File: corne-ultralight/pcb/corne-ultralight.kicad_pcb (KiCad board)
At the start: 2 copper layers, 275.5 x 105.6 mm, 136 parts, among them J2 OLED, J5 Breakaway_Tabs, J7 OLED, SW1 SW_PUSH, SW10 SW_PUSH, SW11 SW_PUSH, SW12 SW_PUSH, SW13 SW_PUSH, SW14 SW_PUSH, SW15 SW_PUSH, SW16 SW_PUSH, SW17 SW_PUSH, SW18 SW_PUSH, SW19 SW_PUSH, SW2 SW_PUSH, SW20 SW_PUSH, SW21 SW_PUSH, SW22 SW_PUSH, SW23 SW_PUSH, SW24 SW_PUSH, SW25 SW_PUSH, SW26 SW_PUSH, SW27 SW_PUSH, SW28 SW_PUSH, SW29 SW_PUSH, SW3 SW_PUSH, SW30 SW_PUSH, SW31 SW_PUSH, SW32 SW_PUSH, SW33 SW_PUSH, SW34 SW_PUSH, SW35 SW_PUSH, SW36 SW_PUSH, SW37 SW_PUSH, SW38 SW_PUSH, SW39 SW_PUSH, SW4 SW_PUSH, SW40 SW_PUSH, SW41 SW_PUSH, SW42 SW_PUSH, SW5 SW_PUSH, SW6 SW_PUSH, SW7 SW_PUSH, SW8 SW_PUSH, SW9 SW_PUSH, U1 ProMicro, U2 ProMicro

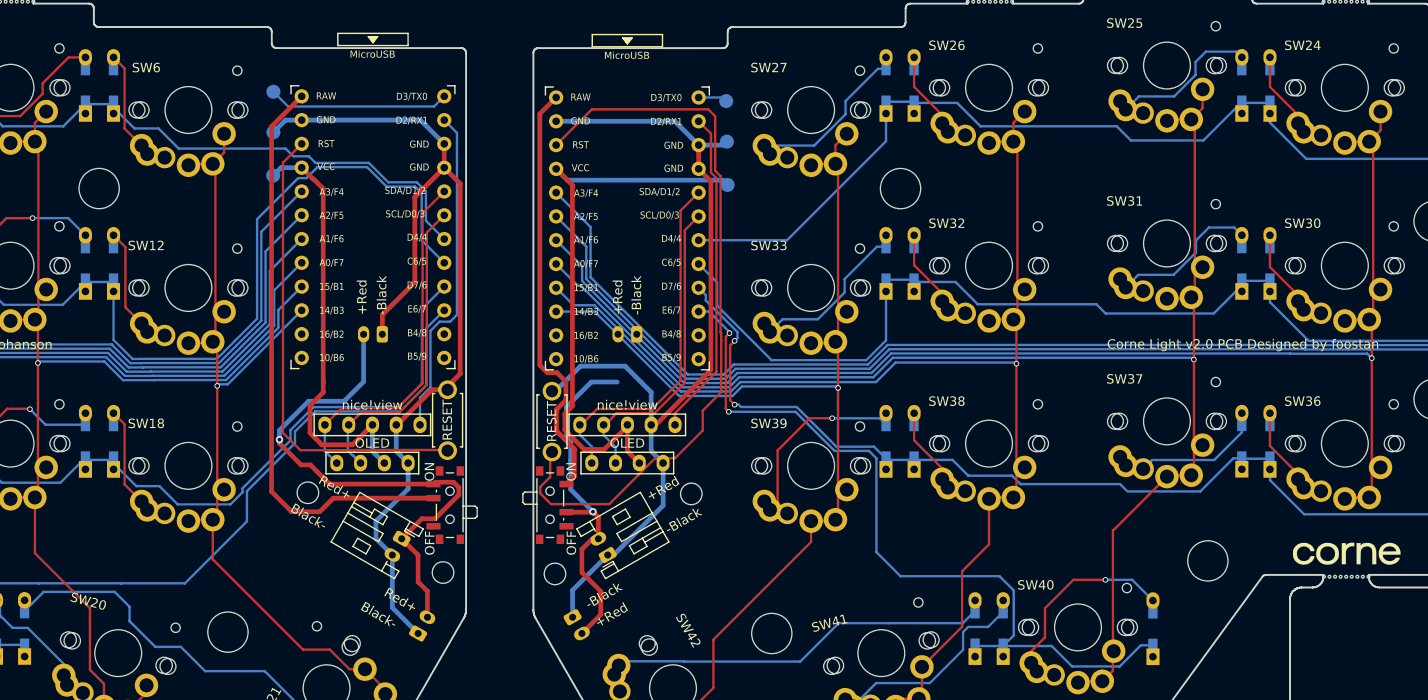
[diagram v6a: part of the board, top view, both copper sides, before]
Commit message: Holes for battery cables
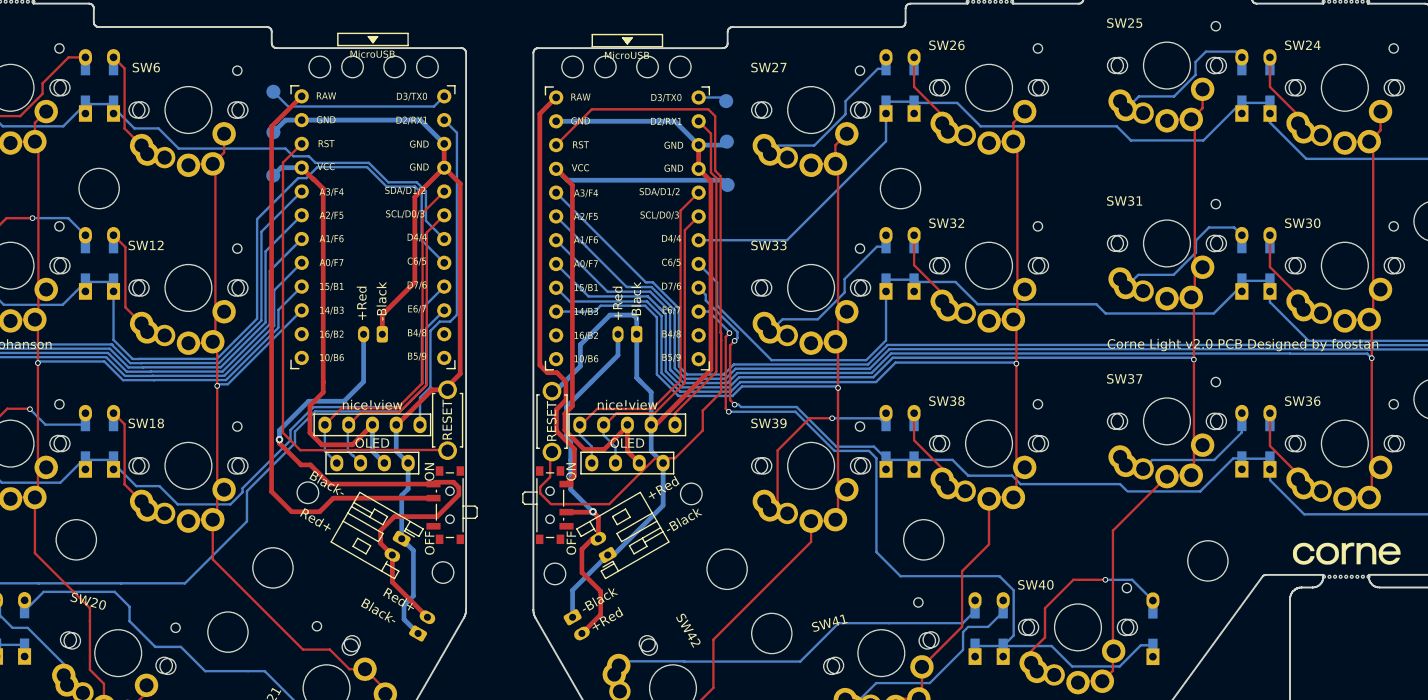
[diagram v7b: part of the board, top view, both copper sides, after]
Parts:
- added Ref**: Val**, kbd:thread_m2, F.Cu at (131.2, 38.9)
- added Ref**: Val**, kbd:spacer_m2, B.Cu at (126.2, 92.4)
- added Ref**: Val**, kbd:spacer_m2, B.Cu at (195.7, 89.4)
- added Ref**: Val**, kbd:spacer_m2, B.Cu at (174.7, 92.6)
- added Ref**: Val**, kbd:thread_m2, F.Cu at (139.2, 38.9)
- added Ref**: Val**, kbd:spacer_m2, B.Cu at (105.2, 89.4)
- added Ref**: Val**, kbd:thread_m2, F.Cu at (166.2, 38.9)
- added Ref**: Val**, kbd:thread_m2, F.Cu at (158.2, 38.9)
- added Ref**: Val**, kbd:thread_m2, F.Cu at (161.7, 38.9)
- added Ref**: Val**, kbd:thread_m2, F.Cu at (169.7, 38.9)
- added Ref**: Val**, kbd:thread_m2, F.Cu at (142.7, 38.9)
- added Ref**: Val**, kbd:thread_m2, F.Cu at (134.7, 38.9)
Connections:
- BATJ2 pad 1: Net-(BATJ1-Pin_2) -> GND
- BATJ2 pad 2: GND -> Net-(BATJ1-Pin_2)
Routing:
- net GNDA: track 94.1 -> 103.6 mm
- net col3_r: track 149.9 -> 154.4 mm
- net col5_r: track 115.8 -> 119.9 mm
- net Net-(BATJ1-Pin_2): track 57.2 -> 60.9 mm
- net col4_r: track 129.4 -> 133.0 mm
- net Net-(BATJ5-Pin_2): track 37.7 -> 41.2 mm
- net col2_r: track 143.5 -> 146.6 mm
- net col1_r: track 161.7 -> 163.3 mm
- net GND: track 100.7 -> 99.3 mm
- net col0_r: track 185.7 -> 186.3 mm

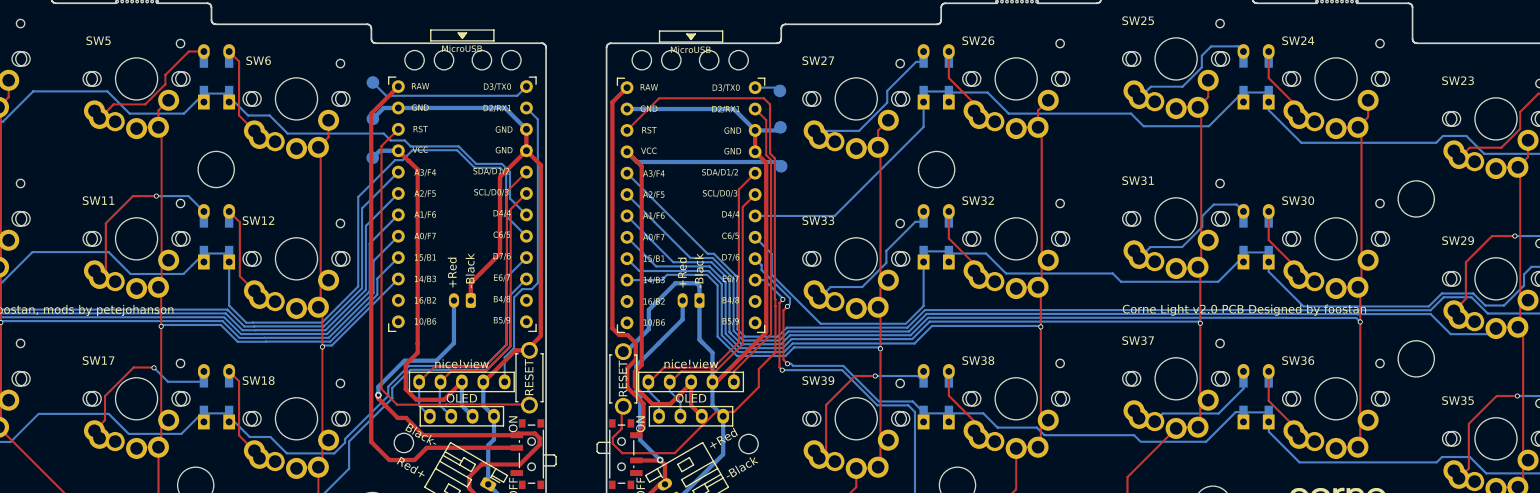
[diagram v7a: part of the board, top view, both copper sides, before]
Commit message: Holes for battery cables
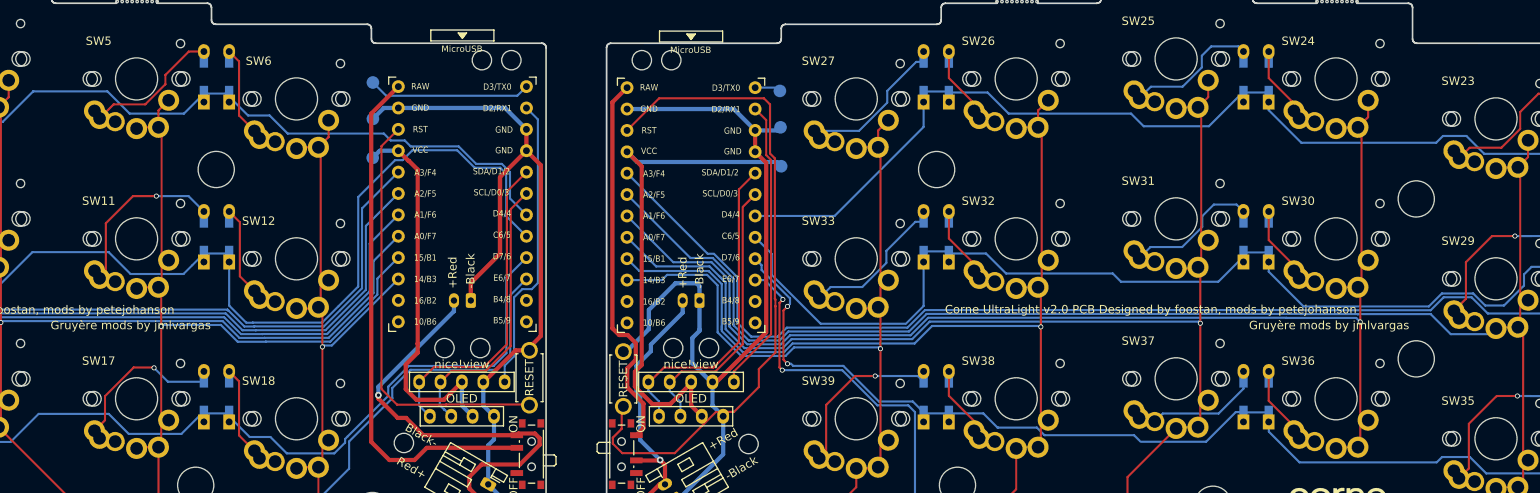
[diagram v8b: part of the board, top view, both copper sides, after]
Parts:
- removed the Ref** at (131.2, 38.9)
- removed the Ref** at (166.2, 38.9)
- removed the Ref** at (169.7, 38.9)
- removed the Ref** at (134.7, 38.9)
- added Ref**: Val**, kbd:thread_m2, F.Cu at (165.7, 73.1)
- added Ref**: Val**, kbd:thread_m2, F.Cu at (134.8, 73.1)
- added Ref**: Val**, kbd:thread_m2, F.Cu at (138.5, 73.1)
- added Ref**: Val**, kbd:thread_m2, F.Cu at (161.9, 73.1)
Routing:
- net Net-(BATJ1-Pin_2): track 60.9 -> 58.7 mm
- net GNDA: track 103.6 -> 104.3 mm
- net row2: track 157.3 -> 157.9 mm
- net row3: track 97.9 -> 98.5 mm
- net col2_r: track 146.6 -> 146.0 mm
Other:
- board text added: "Gruyère mods by jmlvargas"
- board text removed: "Corne Light v2.0 PCB Designed by foostan"
